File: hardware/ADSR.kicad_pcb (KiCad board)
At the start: 2 copper layers, 87 parts, among them J1 Conn_02x05_Counter_Clockwise, U1 TLV9004xRUCR, U10 MCP4921-EP, U11 LM1117-5.0, U2 TL074, U3 TLV9004xRUCR

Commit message: added TLV9004 to library and placement is final
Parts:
- removed C1, C2, C3: 100n, Capacitor_SMD:C_0805_2012Metric_Pad1.18x1.45mm_HandSolder
- removed C4: 10n, Capacitor_SMD:C_0805_2012Metric_Pad1.18x1.45mm_HandSolder
- added c3: 100n, Capacitor_SMD:C_0805_2012Metric_Pad1.18x1.45mm_HandSolder, F.Cu at (172.7, 80.8)
- added c4: 100n, Capacitor_SMD:C_0805_2012Metric_Pad1.18x1.45mm_HandSolder, F.Cu at (172.2, 129.8)
- added c5: 100n, Capacitor_SMD:C_0805_2012Metric_Pad1.18x1.45mm_HandSolder, F.Cu at (212.3, 90.2)
- added c7: 10n, Capacitor_SMD:C_0805_2012Metric_Pad1.18x1.45mm_HandSolder, B.Cu at (181.9, 121.2)
- J1: footprint Connector_PinSocket_2.54mm:PinSocket_2x05_P2.54mm_Vertical -> Connector_PinHeader_2.54mm:PinHeader_2x05_P2.54mm_Vertical
- U1, U3: value TLV9004xRUCR -> TLV9004
- U10: moved to F.Cu
- moved R24 160.4 mm to (218.4, 89.7)
- moved R25 152.7 mm to (218.4, 92.7)
- moved R26 147.1 mm to (203.2, 92.7), turned to 0 degrees
- moved D6 143.9 mm to (227.8, 49.3)
- moved R27 141.5 mm to (185.9, 121.2), turned to 0 degrees
- moved R28 132.6 mm to (178.8, 129.8), turned to 0 degrees
- moved U10 132.2 mm to (185.9, 126.2), turned to 0 degrees
- moved R22 129.1 mm to (209.3, 114.6), turned to 270 degrees
- moved c2 128.6 mm to (216.3, 49.3), turned to 0 degrees
- moved R20 125.7 mm to (209.3, 109.8), turned to 270 degrees
- moved D2 121.9 mm to (160.0, 149.2), turned to 0 degrees
- moved U11 121.2 mm to (197.5, 45.7)
- moved R19 119.5 mm to (212.3, 109.8), turned to 270 degrees
- moved R33 114.1 mm to (178.8, 132.3), turned to 0 degrees
- moved R35 112.8 mm to (178.8, 134.9), turned to 0 degrees
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- renumbered C5 to c6
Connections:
- D5 pad 2: Net-(C5-Pad1) -> Net-(D5-Pad2)
- J1 pad 1: Net-(C5-Pad1) -> Net-(D5-Pad2)
- J1 pad 10: Net-(C5-Pad1) -> Net-(D6-Pad1)
- J1 pad 2: GND -> Net-(D5-Pad2)
- J1 pad 5: Net-(D6-Pad1) -> GND
- J1 pad 6: Net-(D6-Pad1) -> GND
- J1 pad 9: GND -> Net-(D6-Pad1)
- U1 pad 1: Net-(R1-Pad1) -> /A
- U1 pad 12: Net-(R13-Pad2) -> GND
- U1 pad 13: /R -> Net-(R13-Pad2)
- U1 pad 14: /A -> /R
- U1 pad 2: GND -> Net-(R1-Pad1)
- U1 pad 3: +5V -> GND
- U1 pad 4: GND -> +5V
- U1 pad 5: Net-(R11-Pad2) -> GND
- U1 pad 6: /D -> Net-(R11-Pad2)
- U1 pad 7: /S -> /D
- U1 pad 8: Net-(R12-Pad2) -> /S
- U1 pad 9: GND -> Net-(R12-Pad2)
- U11 pad 3: Net-(C5-Pad1) -> +12V
- U3 pad 1: Net-(R15-Pad1) -> /cA
- U3 pad 12: Net-(R21-Pad1) -> GND
- U3 pad 13: /cR -> Net-(R21-Pad1)
- U3 pad 14: /cA -> /cR
- U3 pad 2: GND -> Net-(R15-Pad1)
- U3 pad 3: +5V -> GND
- U3 pad 4: GND -> +5V
- U3 pad 5: Net-(R17-Pad1) -> GND
- U3 pad 6: /cD -> Net-(R17-Pad1)
- U3 pad 7: /cS -> /cD
- U3 pad 8: Net-(R19-Pad1) -> /cS
- U3 pad 9: GND -> Net-(R19-Pad1)
- c6 pad 1: Net-(C5-Pad1) -> +12V
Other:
- board text added: "ADSR"
- board text added: "LOPE"
- board text added: "VC"

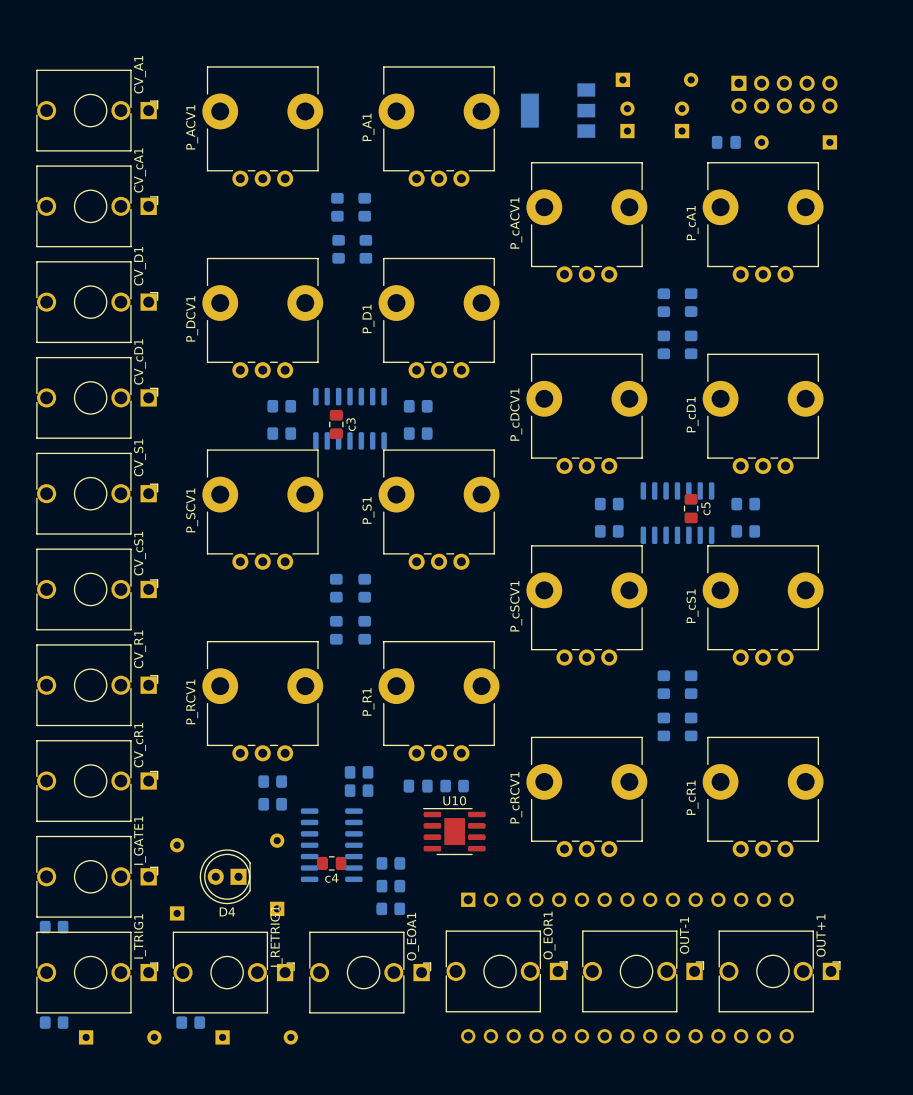
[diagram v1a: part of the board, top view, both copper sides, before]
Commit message: added more puffer caps. im lazy. go autoRoute
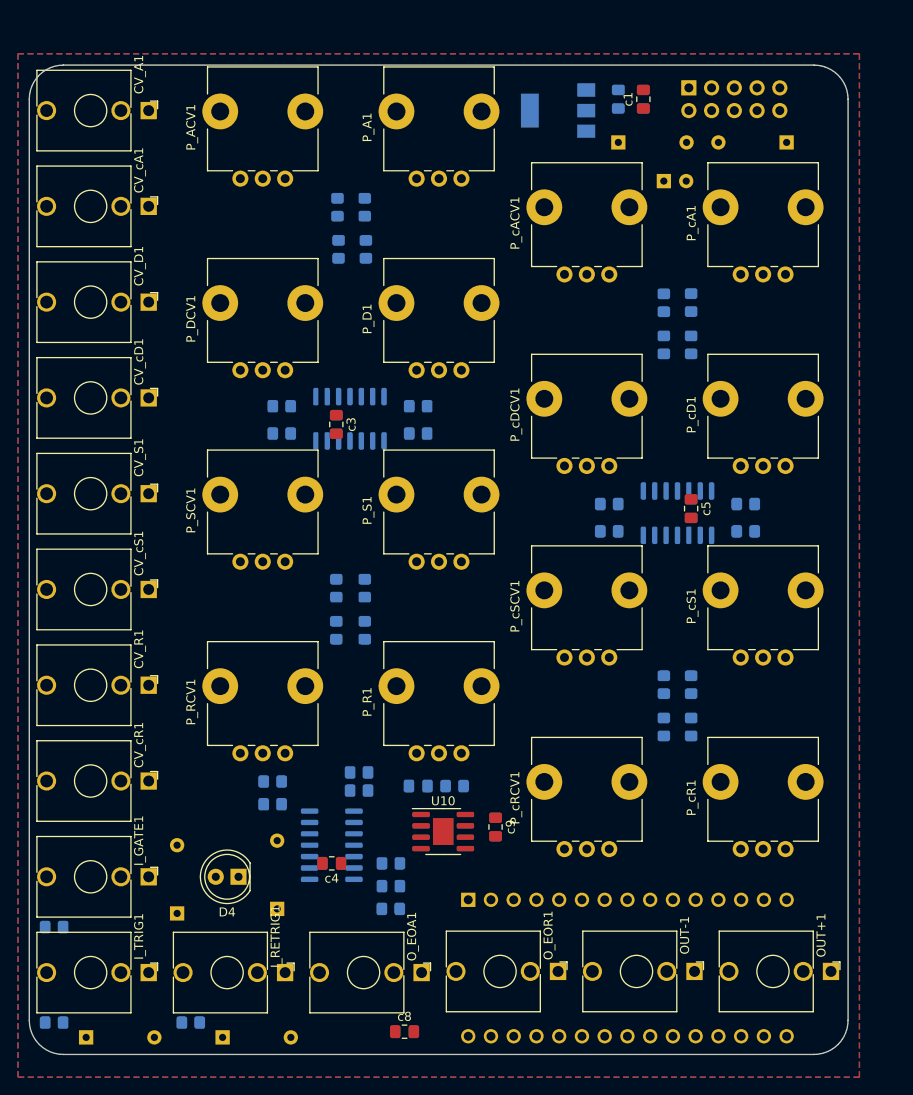
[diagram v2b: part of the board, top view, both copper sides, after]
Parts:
- added c8: 100n, Capacitor_SMD:C_0805_2012Metric_Pad1.18x1.45mm_HandSolder, F.Cu at (180.3, 148.6)
- added c9: 100n, Capacitor_SMD:C_0805_2012Metric_Pad1.18x1.45mm_HandSolder, F.Cu at (190.5, 125.7)
- c1: value 47u -> 100n; footprint Capacitor_THT:CP_Radial_D5.0mm_P2.50mm -> Capacitor_SMD:C_0805_2012Metric_Pad1.18x1.45mm_HandSolder; moved to F.Cu
- moved c2 13.0 mm to (204.2, 44.5), turned to 90 degrees
- moved D5 7.00 mm to (204.2, 49.3)
- moved c6 6.91 mm to (209.3, 53.6), turned to 0 degrees
- moved J1 5.61 mm to (212.1, 43.2)
- moved c1 5.59 mm to (207.0, 44.5)
- moved D6 4.83 mm to (223.0, 49.3)
- moved U10 1.27 mm to (184.7, 126.2)
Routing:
- added copper zone on B.Cu, net GND
- added copper zone on F.Cu, net GND
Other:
- board outline added: 91.4 x 110.5 mm

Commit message: hardware done
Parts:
- added R36: 50k, Potentiometers:Potentiometer_Trimmer_Bourns_3296W, B.Cu at (186.7, 101.1)
- R27: value 1.5k -> 22k
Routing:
- net GND: track 0.00 -> 666.4 mm, vias 0 -> 1
- net +5V: track 0.00 -> 233.2 mm, vias 0 -> 4
- net -5V: track 0.00 -> 196.5 mm
- net /A: track 0.00 -> 131.3 mm
- net -12V: track 0.00 -> 125.3 mm, vias 0 -> 1
- net /R: track 0.00 -> 109.1 mm, vias 0 -> 1
- net +12V: track 0.00 -> 107.4 mm, vias 0 -> 1
- net /cD: track 0.00 -> 99.1 mm
- net /S: track 0.00 -> 97.2 mm
- net /D: track 0.00 -> 94.9 mm, vias 0 -> 1
- net Net-(CV_cD1-PadT): track 0.00 -> 87.6 mm, vias 0 -> 1
- net Net-(OUT+1-PadT): track 0.00 -> 83.9 mm
- net /cS: track 0.00 -> 82.7 mm
- net Net-(CV_cS1-PadT): track 0.00 -> 74.4 mm
- net /GATE: track 0.00 -> 72.8 mm
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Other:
- net class saft added: clearance 0.2, trace_width 0.4, via_dia 0.8, via_drill 0.4
